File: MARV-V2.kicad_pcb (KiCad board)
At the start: 4 copper layers, 50 x 50 mm, 139 parts, among them J10 DBG pads (SWCLK SWDIO GND), J11 microSD, Molex 104031-0811 pu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, J12 PWM5-8 signals, row 1, J13 Servo 5 V (5V_IN), row 2, J14 GND, row 3, J15 BUZZER pads (5V BZ-), J16 SPARE IO 2x6 (see note), J3 ESC pads (CURR TX M4 M3 M2 M1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, J4 USB_C_PROGRAM_POWER, J6 UART_GPS (DS-009: VCC/TX/RX/G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, J7 UART_ELRS (DS-009: VCC/TX/RX/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, J9 I2C_MAG (DS-009: VCC/SCL/SDA/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, Q20 2N7002, SW1 RESET (RUN to GND), SW2 BOOTSEL (via R24), U12 TPS7A2033PDBVR, U20 RP2354B, U21 ICM-45686 6-axis IMU, U22 BMP581 barometer, U23 ADXL375 high-g accelerometer, U24 W25Q64JVSSIQ, 64 Mbit QSPI NOR, U25 TPS2121RUXR, U26 AP63205WU-7, U7 TPS62913RPUR, U8 USBLC6-2SC6, Y1 12 MHz ABM8-272-T3, CL 10 pF

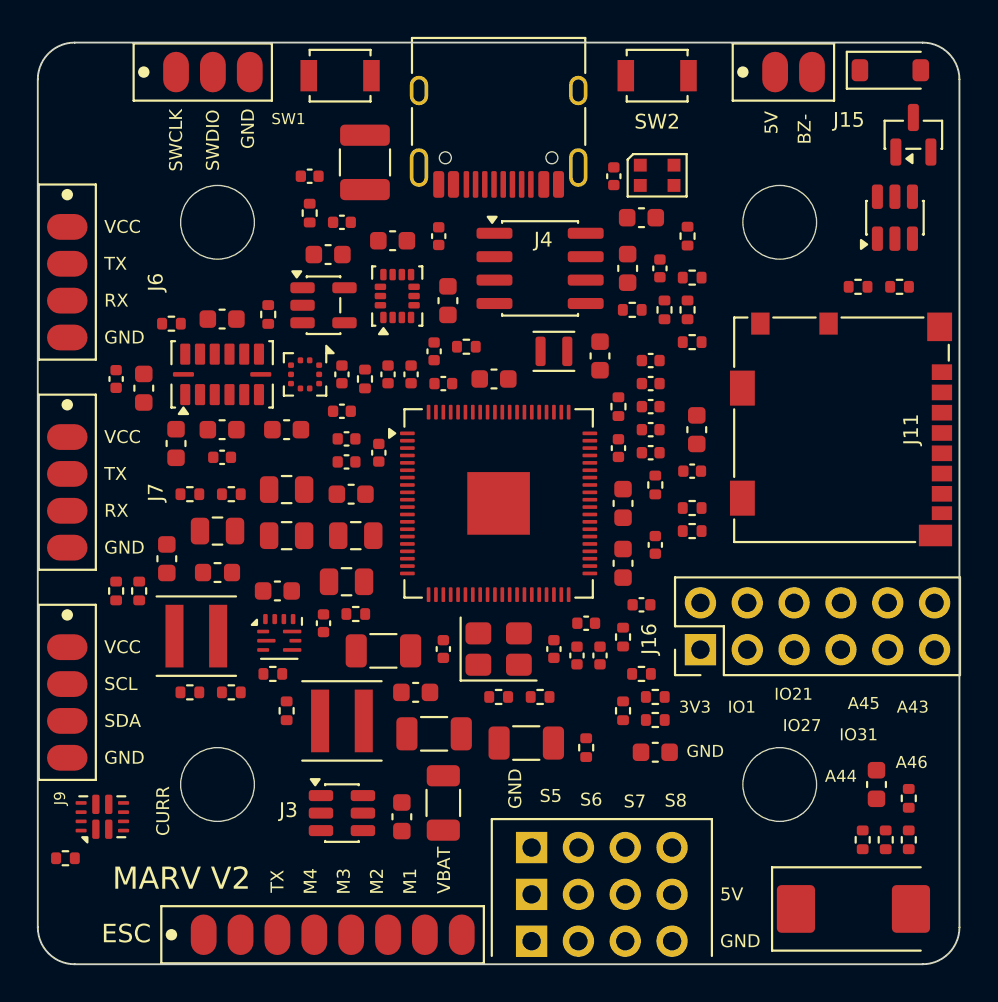
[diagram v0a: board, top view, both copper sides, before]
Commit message: Remove buzzer; passives to 0201/0402; GPIO28 to spare-IO block
Buzzer pads J15, driver Q20/D22/R33/R34 and the BUZZ nets removed; GPIO28
now terminates on J16 pin 12 (was a second GND). Resistors 0201, caps
<= 4.7 uF 0402, 22 uF/10 V 0603, 22 uF/25 V and 10 uF/50 V 0805, 47 uF
0805; USB net-class clearance 0.18 mm so the 0201 series resistors on the
pair pass DRC. Board regenerated at 50 x 50 mm (courtyard fill 63.5 %);
DRC unrouted-only. 134 components, 105 nets; ERC 0/0, 213 pin mappings,
run_power_checks PASS, audit 134/134.

Co-Authored-By: Claude Fable 5.1 <noreply@anthropic.com>
Claude-Session: https://claude.ai/code/session_01U6Ud7JA3CDTJZVcZZr5sx1
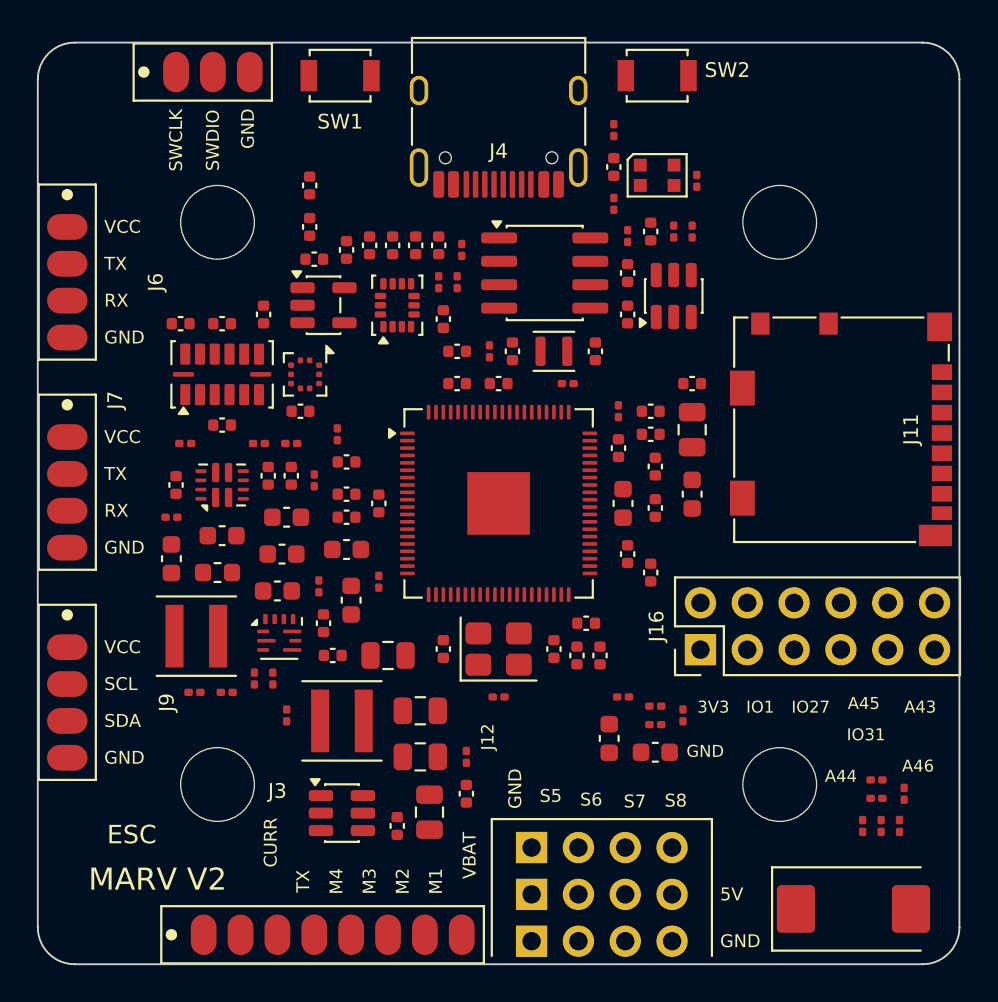
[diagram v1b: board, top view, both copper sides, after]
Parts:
- removed D22: flyback across the buzzer pads, Diode_SMD:D_SOD-123
- removed J15: BUZZER pads (5V BZ-), MARV_Packages:PadRow_1x02_P2.00mm
- removed Q20: 2N7002, Package_TO_SOT_SMD:SOT-23
- removed R33: 1k, gate series, Resistor_SMD:R_0402_1005Metric
- removed R34: 100k, gate pull-down, Resistor_SMD:R_0402_1005Metric
- C10, C11, C12: value 22u / 10 V X7S, 1st-stage COUT -> 22u / 10 V X5R 0603 GRM188R61A226ME15, 1st-stage COUT (~40% DC-bias loss at 3.3 V); footprint Capacitor_SMD:C_0805_2012Metric -> Capacitor_SMD:C_0603_1608Metric
- C13: value 470n / 16 V X7R 0603, NR/SS soft-start + noise filter (5 ms) -> 470n / 16 V X7R 0402, NR/SS soft-start + noise filter (5 ms); footprint Capacitor_SMD:C_0603_1608Metric -> Capacitor_SMD:C_0402_1005Metric
- C23, C24: value 22u / 10 V X7S, 2nd-stage Cf (post-bead) -> 22u / 10 V X5R 0603 GRM188R61A226ME15, 2nd-stage Cf post-bead (~40% DC-bias loss at 3.3 V); footprint Capacitor_SMD:C_0805_2012Metric -> Capacitor_SMD:C_0603_1608Metric
- C25: value 1u / 10 V X7R 0603, LDO input -> 1u / 10 V X7R 0402, LDO input; footprint Capacitor_SMD:C_0603_1608Metric -> Capacitor_SMD:C_0402_1005Metric
- C26: value 1u / 10 V X7R 0603, LDO output, ESR <=100 mOhm -> 1u / 10 V X7R 0402, LDO output, ESR <=100 mOhm; footprint Capacitor_SMD:C_0603_1608Metric -> Capacitor_SMD:C_0402_1005Metric
- C39: value 4.7u / 10 V X7R 0603, VREG_VIN -> 4.7u / 10 V X5R 0402, VREG_VIN; footprint Capacitor_SMD:C_0603_1608Metric -> Capacitor_SMD:C_0402_1005Metric
- C41: value 4.7u / 10 V X7R 0603, VREG_AVDD -> 4.7u / 10 V X5R 0402, VREG_AVDD; footprint Capacitor_SMD:C_0603_1608Metric -> Capacitor_SMD:C_0402_1005Metric
- C45: value 4.7u / 10 V X7R 0603, DVDD bulk -> 4.7u / 10 V X5R 0402, DVDD bulk; footprint Capacitor_SMD:C_0603_1608Metric -> Capacitor_SMD:C_0402_1005Metric
- C51: value 1u / 10 V X7R 0603, U21 VDD -> 1u / 10 V X7R 0402, U21 VDD; footprint Capacitor_SMD:C_0603_1608Metric -> Capacitor_SMD:C_0402_1005Metric
- C53: value 1u / 10 V X7R 0603, U21 VDDIO -> 1u / 10 V X7R 0402, U21 VDDIO; footprint Capacitor_SMD:C_0603_1608Metric -> Capacitor_SMD:C_0402_1005Metric
- C55: value 1u / 10 V X7R 0603, U22 VDD -> 1u / 10 V X7R 0402, U22 VDD; footprint Capacitor_SMD:C_0603_1608Metric -> Capacitor_SMD:C_0402_1005Metric
- C57: value 1u / 10 V X7R 0603, U22 VDDIO -> 1u / 10 V X7R 0402, U22 VDDIO; footprint Capacitor_SMD:C_0603_1608Metric -> Capacitor_SMD:C_0402_1005Metric
- C59: value 1u / 10 V X7R 0603, U23 VS -> 1u / 10 V X7R 0402, U23 VS; footprint Capacitor_SMD:C_0603_1608Metric -> Capacitor_SMD:C_0402_1005Metric
- C61: value 1u / 10 V X7R 0603, U23 VDD_IO -> 1u / 10 V X7R 0402, U23 VDD_IO; footprint Capacitor_SMD:C_0603_1608Metric -> Capacitor_SMD:C_0402_1005Metric
- C63: value 1u / 10 V X7R 0603, U24 VCC -> 1u / 10 V X7R 0402, U24 VCC; footprint Capacitor_SMD:C_0603_1608Metric -> Capacitor_SMD:C_0402_1005Metric
- C66: value 47u / 6.3 V X5R, at the socket -> 47u / 6.3 V X5R 0805, at the socket; footprint Capacitor_SMD:C_1210_3225Metric -> Capacitor_SMD:C_0805_2012Metric
- C7: value 1u / 10 V X7R 0603 -> 1u / 10 V X7R 0402; footprint Capacitor_SMD:C_0603_1608Metric -> Capacitor_SMD:C_0402_1005Metric
- C73: value 10u / 50 V X7R, VIN bulk -> 10u / 50 V X5R 0805 GRM21BR61H106KE43, VIN bulk; footprint Capacitor_SMD:C_1206_3216Metric -> Capacitor_SMD:C_0805_2012Metric
- C74: value 100n / 50 V X7R, VIN HF bypass -> 100n / 50 V X7R 0402, VIN HF bypass; footprint Capacitor_SMD:C_0603_1608Metric -> Capacitor_SMD:C_0402_1005Metric
- C75: value 100n / 50 V X7R, bootstrap -> 100n / 50 V X7R 0402, bootstrap; footprint Capacitor_SMD:C_0603_1608Metric -> Capacitor_SMD:C_0402_1005Metric
- C76, C77: value 22u / 25 V X5R, buck COUT -> 22u / 25 V X5R 0805 GRM21BR61E226ME44, buck COUT; footprint Capacitor_SMD:C_1206_3216Metric -> Capacitor_SMD:C_0805_2012Metric
- C80: value 22u / 25 V X5R, buck COUT (3rd: >=44 uF after DC-bias derating, AP63205 EVB guide) -> 22u / 25 V X5R 0805 GRM21BR61E226ME44, buck COUT (3rd: >=44 uF after DC-bias derating, AP63205 EVB guide); footprint Capacitor_SMD:C_1206_3216Metric -> Capacitor_SMD:C_0805_2012Metric
- R10, R20, R21, R22, R23, R24, R25, R26, R27, R28, R29, R30, R35, R36, R37, R38, R39, R4, R40, R41, R42, R43, R44, R45, R46, R47, R48, R5, R50, R51, R52, R53, R54, R55, R7, R8, R9: footprint Resistor_SMD:R_0402_1005Metric -> Resistor_SMD:R_0201_0603Metric
- moved C66 22.9 mm to (110.5, 96.0)
- moved R41 19.3 mm to (122.0, 115.8), turned to 90 degrees
- moved U25 19.1 mm to (85.0, 99.0)
- moved R26 18.8 mm to (83.5, 110.2)
- moved R40 16.8 mm to (120.5, 115.0)
- moved C56 16.7 mm to (94.2, 86.0)
- moved C57 15.8 mm to (89.8, 82.8)
- moved C21 14.7 mm to (106.0, 112.8)
- moved R47 14.7 mm to (91.2, 96.2)
- moved R48 14.7 mm to (96.8, 88.0), turned to 90 degrees
- moved R45 14.6 mm to (88.8, 96.8)
- moved C72 14.0 mm to (88.8, 98.5), turned to 90 degrees
- moved R10 13.6 mm to (93.5, 104.2)
- moved C54 13.4 mm to (89.8, 85.0), turned to 90 degrees
- moved C40 13.3 mm to (93.5, 100.0)
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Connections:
- J16 pad 12: GND -> IO_GPIO28
- U20 pad 36: BUZZ_PWM -> IO_GPIO28
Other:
- board text removed: "BZ-"
- board text removed: "IO21"

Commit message: IO array replaces bus pad rows; PINOUT.md pin plan; test points; ESC/battery docs
Left edge is now one 2 x 16 through-hole IO array (J6, signal | 5V/3V3/GND
rows, madflight-style) carrying GPS/ELRS/MAG and the ten spare GPIOs; the
J6/J7/J9 pad rows and the J16 block are gone. ESC pad row J3 and DBG pads
J10 stay; servo block J12-J14 stays beside the ESC row. TP1-TP10 1 mm test
points on the sensor SPI, chip selects and interrupts.

PINOUT.md records every GPIO's function and alternates from RP2350
datasheet Table 3, the spare-pin roles (I2C0 on 44/45, SPI1 on 46/47/28,
ADC3-7) and the peripheral ledger; check_power_netlist.py now asserts all
48 GPIO nets against it.

DESIGN_SPEC: ESC connection table, IO array table, test points, battery
monitoring (VBAT_SENSE + ESC current; INA226 rejected), edge allocation.
setup_pcb.py vendors the header footprints with project-local 3D models;
board 50 x 50 mm (48 collides with the grommet keepouts), DRC unrouted-only.
141 components, 105 nets, 231 pin mappings; ERC 0/0, ngspice PASS,
audit 141/141.

Co-Authored-By: Claude Fable 5.1 <noreply@anthropic.com>
Claude-Session: https://claude.ai/code/session_01U6Ud7JA3CDTJZVcZZr5sx1
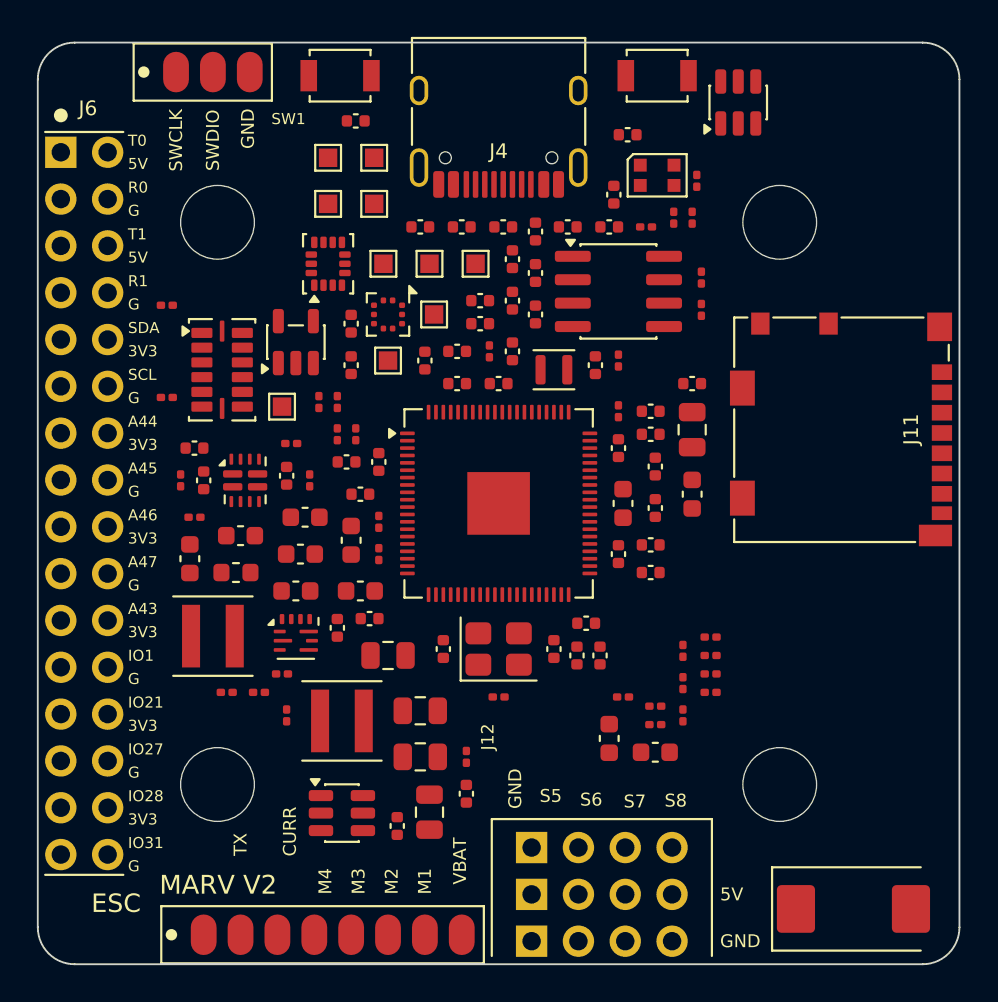
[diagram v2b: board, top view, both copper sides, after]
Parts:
- removed J16: SPARE IO 2x6 (see note), Connector_PinHeader_2.54mm:PinHeader_2x06_P2.54mm_Vertical
- removed J7: UART_ELRS (DS-009: VCC/TX/RX/GND), MARV_Packages:PadRow_1x04_P2.00mm
- removed J9: I2C_MAG (DS-009: VCC/SCL/SDA/GND), MARV_Packages:PadRow_1x04_P2.00mm
- added TP1: TP SENS_SCK, TestPoint:TestPoint_Pad_1.0x1.0mm, F.Cu at (93.8, 87.0)
- added TP10: TP HG_ACC_INT, TestPoint:TestPoint_Pad_1.0x1.0mm, F.Cu at (93.2, 83.8)
- added TP2: TP SENS_MOSI, TestPoint:TestPoint_Pad_1.0x1.0mm, F.Cu at (90.8, 83.8)
- added TP3: TP SENS_MISO, TestPoint:TestPoint_Pad_1.0x1.0mm, F.Cu at (96.2, 87.0)
- added TP4: TP IMU_CS, TestPoint:TestPoint_Pad_1.0x1.0mm, F.Cu at (90.8, 81.2)
- added TP5: TP BARO_CS, TestPoint:TestPoint_Pad_1.0x1.0mm, F.Cu at (94.0, 92.2)
- added TP6: TP HG_ACC_CS, TestPoint:TestPoint_Pad_1.0x1.0mm, F.Cu at (88.2, 94.8)
- added TP7: TP IMU_INT1, TestPoint:TestPoint_Pad_1.0x1.0mm, F.Cu at (93.2, 81.2)
- added TP8: TP IMU_INT2, TestPoint:TestPoint_Pad_1.0x1.0mm, F.Cu at (98.8, 87.0)
- added TP9: TP BARO_INT, TestPoint:TestPoint_Pad_1.0x1.0mm, F.Cu at (96.5, 89.8)
- J6: value UART_GPS (DS-009: VCC/TX/RX/GND) -> IO array 2x16 (signal | power/GND); footprint MARV_Packages:PadRow_1x04_P2.00mm -> MARV_Packages:PinHeader_2x16_P2.54mm_Vertical_IOArray
- moved C61 18.0 mm to (102.0, 89.8), turned to 90 degrees
- moved R51 17.9 mm to (82.0, 94.2), turned to 0 degrees
- moved C26 16.1 mm to (98.0, 85.0)
- moved R50 15.8 mm to (82.0, 89.2), turned to 0 degrees
- moved R39 13.8 mm to (111.5, 108.2), turned to 0 degrees
- moved R41 13.5 mm to (111.5, 107.2), turned to 0 degrees
- moved C45 12.7 mm to (106.5, 102.8), turned to 90 degrees
- moved R40 12.6 mm to (110.0, 108.0), turned to 90 degrees
- moved R37 12.4 mm to (111.5, 109.2), turned to 0 degrees
- moved R38 12.2 mm to (110.0, 109.8), turned to 90 degrees
- moved C25 12.0 mm to (95.8, 85.0)
- moved C50 11.8 mm to (99.0, 89.0), turned to 0 degrees
- moved C57 11.7 mm to (100.8, 86.8)
- moved U8 11.1 mm to (113.0, 78.2)
- moved R36 11.0 mm to (111.5, 110.2), turned to 0 degrees
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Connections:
- J6 pad 1: V5_SYS -> GPS_RX
- J6 pad 2: GPS_RX -> V5_SYS
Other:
- board text added: "A47"
- board text added: "G"
- board text added: "IO21"
- board text added: "IO28"
- board text added: "R0"
- board text added: "R1"
- board text added: "T0"
- board text added: "T1"
- board text removed: "RX"
- board text removed: "VCC"

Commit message: Madflight-style layout: 48.7 x 41.2 mm, ESC row left, 3x14 IO block right
Board re-laid out to the madflight FC3v2 arrangement and shrunk from the
50 x 50 square: rectangle 48.7 x 41.2 mm, 30.5 mm mounting square offset
(7.0 mm left margin for the vertical ESC pad row J3, 11.2 mm right margin
for the IO block), grommet keepout Ø6.5. The IO block is three abutting
1x14 rows J6/J7/J8 (signal | 5V/3V3 | GND per row): T0 R0 T1 R1 SDA SCL
S5-S8 A44-A47. The servo block and the 2x16 array are gone (actuators sheet
removed); GPIO 1/21/27/28/31/43 are no-connect (PINOUT.md, checker
updated). microSD ejects off the top edge, USB-C/RESET/BOOT/LED/DBG on the
bottom edge, sensors + test points between the MCU and the IO block.

Courtyard fill 75.7 %, 0 fit/geometry problems, DRC unrouted-only.
140 components; ERC 0/0, checker PASS, ngspice PASS, audit 140/140.
Known: the board-level silk labels on the ESC row and IO block are
mis-nudged by the label fixer (CURR/VBAT/A47 hidden) — silk pass pending.

Co-Authored-By: Claude Fable 5.1 <noreply@anthropic.com>
Claude-Session: https://claude.ai/code/session_01U6Ud7JA3CDTJZVcZZr5sx1
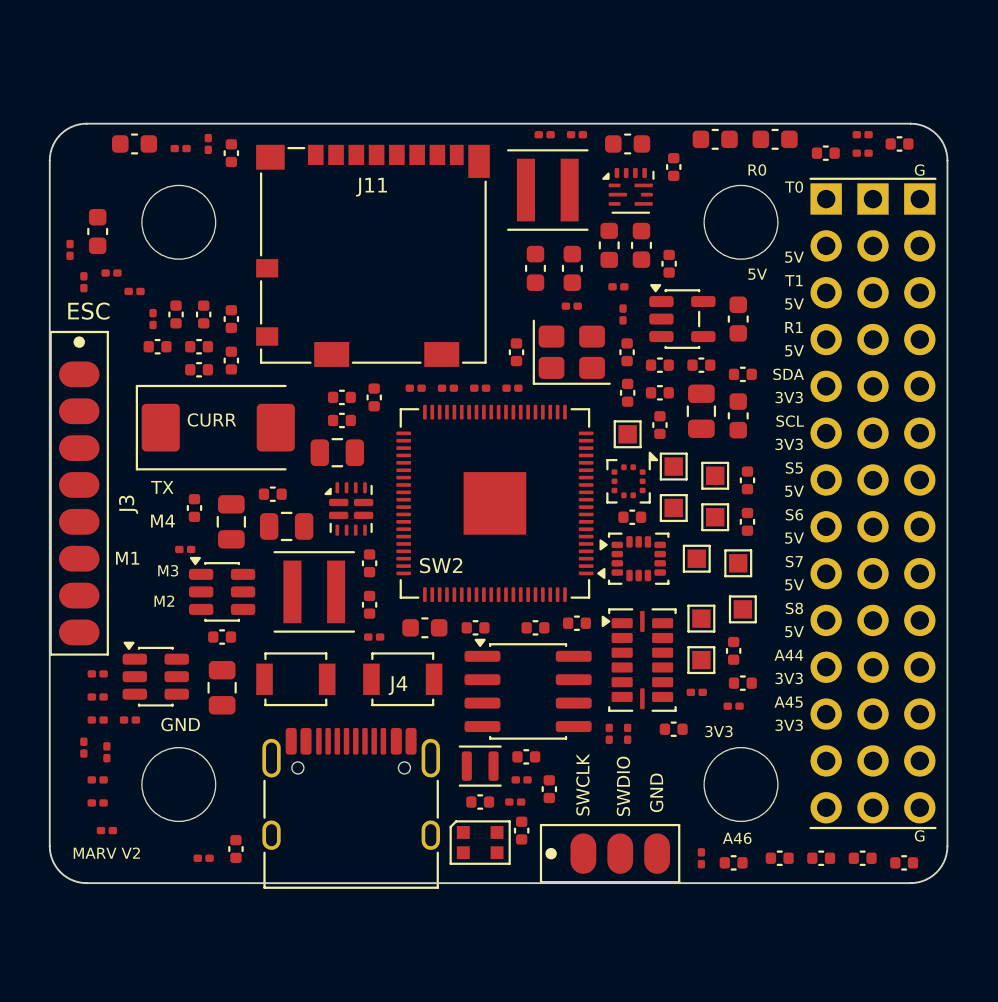
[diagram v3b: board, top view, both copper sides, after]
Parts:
- removed J12: PWM5-8 signals, row 1, MARV_Packages:PinHeader_1x04_P2.54mm_Vertical_ServoRow
- removed J13: Servo 5 V (5V_IN), row 2, MARV_Packages:PinHeader_1x04_P2.54mm_Vertical_ServoRow
- removed J14: GND, row 3, MARV_Packages:PinHeader_1x04_P2.54mm_Vertical_ServoRow
- added J7: IO array power column (5V / 3V3 per row), MARV_Packages:PinHeader_1x14_P2.54mm_Vertical_IORow, F.Cu at (120.3, 83.5)
- added J8: IO array GND column (board edge), MARV_Packages:PinHeader_1x14_P2.54mm_Vertical_IORow, F.Cu at (122.8, 83.5)
- J6: value IO array 2x16 (signal | power/GND) -> IO array signal column (innermost); footprint MARV_Packages:PinHeader_2x16_P2.54mm_Vertical_IOArray -> MARV_Packages:PinHeader_1x14_P2.54mm_Vertical_IORow
- moved J10 47.8 mm to (106.6, 119.0)
- moved R4 47.6 mm to (78.8, 117.8), turned to 0 degrees
- moved U8 44.4 mm to (81.4, 109.4), turned to 0 degrees
- moved C20 43.4 mm to (80.2, 80.5)
- moved C19 43.2 mm to (84.8, 95.9)
- moved R22 43.1 mm to (84.0, 119.2), turned to 0 degrees
- moved R50 41.7 mm to (111.0, 119.2), turned to 90 degrees
- moved J6 41.6 mm to (117.8, 83.5)
- moved R5 41.3 mm to (78.8, 113.5)
- moved C7 41.0 mm to (85.8, 118.8)
- moved R23 40.9 mm to (80.0, 111.8), turned to 0 degrees
- moved R51 40.0 mm to (119.8, 81.0)
- moved J4 39.1 mm to (92.0, 117.0), turned to 0 degrees
- moved C21 39.1 mm to (78.2, 85.2)
- moved C60 37.7 mm to (122.0, 119.5), turned to 0 degrees
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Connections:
- J6 pad 10: V3V3_SYS -> PWM8
- J6 pad 11: MAG_SCL -> IO_GPIO44
- J6 pad 12: GND -> IO_GPIO45
- J6 pad 13: IO_GPIO44 -> IO_GPIO46
- J6 pad 14: V3V3_SYS -> IO_GPIO47
- J6 pad 2: V5_SYS -> GPS_TX
- J6 pad 3: GPS_TX -> ELRS_RX
- J6 pad 4: GND -> ELRS_TX
- J6 pad 5: ELRS_RX -> MAG_SDA
- J6 pad 6: V5_SYS -> MAG_SCL
- J6 pad 7: ELRS_TX -> PWM5
- J6 pad 8: GND -> PWM6
- J6 pad 9: MAG_SDA -> PWM7
- U20 pad 21: IO_GPIO21 -> unconnected-(U20-GPIO21-Pad21)
- U20 pad 28: IO_GPIO27 -> unconnected-(U20-GPIO27-Pad28)
- U20 pad 36: IO_GPIO28 -> unconnected-(U20-GPIO28-Pad36)
- U20 pad 39: IO_GPIO31 -> unconnected-(U20-GPIO31-Pad39)
- U20 pad 54: IO_GPIO43 -> unconnected-(U20-GPIO43/ADC3-Pad54)
- U20 pad 78: IO_GPIO1 -> unconnected-(U20-GPIO1-Pad78)
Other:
- board size 50 x 50 mm -> 48.7 x 41.2 mm
- board text removed: "A43"
- board text removed: "A47"
- board text removed: "IO1"
- board text removed: "IO21"
- board text removed: "IO27"
- board text removed: "IO28"
- board text removed: "IO31"
- board text removed: "VBAT"
